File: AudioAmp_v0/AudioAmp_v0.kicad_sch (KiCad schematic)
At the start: 2 parts, among them J1 Conn_01x02_Pin, U1 MAU108

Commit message: 電源回路完成
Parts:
- added C1: 100u, symbol Device:C_Polarized
- added C2, C6, C7: 10u, Capacitor_SMD:C_0805_2012Metric, symbol Device:C
- added C3, C4, C5: 0.1u, Capacitor_SMD:C_0603_1608Metric, symbol Device:C
- J1: footprint (none) -> Connector_Molex:Molex_SPOX_5268-02A_1x02_P2.50mm_Horizontal
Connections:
- net +5V: now also U1.1 (+VIN), C1.1, C2.1, C3.1
- net GND: now also U1.2 (-Vin), U1.5 (Common), C1.2, C2.2, C3.2, C4.2, C5.1, C6.2, C7.1
- net +12V: now reaches U1.4 (-VOUT)
- net +12V: now also C4.1, C6.1
- net -12V: now reaches U1.6 (+Vout)
- net -12V: now also C5.2, C7.2
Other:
- moved on the sheet: U1

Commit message: アンプ回路ちょっと
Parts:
- added J2: AudioJack3, Connector_Audio:Jack_3.5mm_Switronic_ST-005-G_horizontal, symbol Connector_Audio:AudioJack3
- added RV1: R_Potentiometer_Dual, symbol Device:R_Potentiometer_Dual
- added U2: NJM5532, Package_DIP:DIP-8_W7.62mm, symbol Amplifier_Operational:NJM5532
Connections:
- net GND: now also J2.S
- new net: U2.1, U2.5 (+)
- new net: U2.6 (-), U2.7
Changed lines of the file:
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@@
+    (stroke (width 0) (type default))
+  )
+  (wire (pts (xy 90.17 119.38) (xy 90.17 124.46))
+    (stroke (width 0) (type default))
+  )
+  (wire (pts (xy 33.02 129.54) (xy 34.29 129.54))
     (stroke (width 0) (type default))
   )
@@
     (stroke (width 0) (type default))
   )
-  (wire (pts (xy 38.1 72.39) (xy 43.18 72.39))
+  (wire (pts (xy 87.63 128.27) (xy 87.63 114.3))
     (stroke (width 0) (type default))
   )
@@
     (stroke (width 0) (type default))
   )
+  (wire (pts (xy 90.17 124.46) (xy 107.95 124.46))
+    (stroke (width 0) (type default))
+  )
   (wire (pts (xy 118.11 81.28) (xy 128.27 81.28))
     (stroke (width 0) (type default))
@@
     (stroke (width 0) (type default))
   )
-  (wire (pts (xy 44.45 74.93) (xy 38.1 74.93))
+  (wire (pts (xy 87.63 114.3) (xy 90.17 114.3))
+    (stroke (width 0) (type default))
+  )
+  (wire (pts (xy 41.91 74.93) (xy 38.1 74.93))
+    (stroke (width 0) (type default))
+  )
+  (wire (pts (xy 107.95 124.46) (xy 107.95 116.84))
     (stroke (width 0) (type default))
   )
@@
     (stroke (width 0) (type default))
   )
+  (wire (pts (xy 86.36 128.27) (xy 87.63 128.27))
+    (stroke (width 0) (type default))
+  )
   (wire (pts (xy 118.11 63.5) (xy 128.27 63.5))
     (stroke (width 0) (type default))
@@
     (stroke (width 0) (type default))
   )
-  (wire (pts (xy 44.45 68.58) (xy 44.45 74.93))
-    (stroke (width 0) (type default))
-  )
   (wire (pts (xy 114.3 76.2) (xy 114.3 81.28))
     (stroke (width 0) (type default))
@@
     (stroke (width 0) (type default))
   )
+  (wire (pts (xy 38.1 72.39) (xy 41.91 72.39))
+    (stroke (width 0) (type default))
+  )
   (wire (pts (xy 72.39 68.58) (xy 81.28 68.58))
     (stroke (width 0) (type default))
   )
-  (wire (pts (xy 43.18 72.39) (xy 43.18 77.47))
+  (wire (pts (xy 107.95 116.84) (xy 105.41 116.84))
     (stroke (width 0) (type default))
   )
@@
     )
   )
+  (symbol (lib_id "Amplifier_Operational:NJM5532") (at 68.58 92.71 0) (unit 3)
+    (in_bom yes) (on_board yes) (dnp no) (fields_autoplaced)
+    (property "Reference" "U2" (at 67.31 91.44 0)
+      (effects (font (size 1.27 1.27)) (justify left))
+    )
+    (property "Value" "NJM5532" (at 67.31 93.98 0)
+      (effects (font (size 1.27 1.27)) (justify left))
+    )
+    (property "Footprint" "Package_DIP:DIP-8_W7.62mm" (at 68.58 92.71 0)
+      (effects (font (size 1.27 1.27)) hide)
+    )
+    (property "Datasheet" "http://www.njr.com/semicon/PDF/NJM5532_E.pdf" (at 68.58 92.71 0)
+      (effects (font (size 1.27 1.27)) hide)
+    )
+    (pin "1")
+    (pin "8")
+    (pin "4")
+    (pin "6")
+    (pin "7")
+    (pin "3")
+    (pin "5")
+    (pin "2")
+    (instances
+      (project "AudioAmp_v0"
+        (path "/4f57bce5-a0af-4dee-a148-d94d96167cd8"
+          (reference "U2") (unit 3)
+        )
+      )
+    )
+  )
   (symbol (lib_id "power:+5V") (at 58.42 67.31 0) (unit 1)
     (in_bom yes) (on_board yes) (dnp no) (fields_autoplaced)
@@
     )
   )
-  (symbol (lib_id "power:+5V") (at 44.45 68.58 0) (unit 1)
-    (in_bom yes) (on_board yes) (dnp no) (fields_autoplaced)
-    (property "Reference" "#PWR02" (at 44.45 72.39 0)
-      (effects (font (size 1.27 1.27)) hide)
-    )
-    (property "Value" "+5V" (at 44.45 63.5 0)
-      (effects (font (size 1.27 1.27)))
-    )
-    (property "Footprint" "" (at 44.45 68.58 0)
-      (effects (font (size 1.27 1.27)) hide)
-    )
-    (property "Datasheet" "" (at 44.45 68.58 0)
+  (symbol (lib_id "power:+5V") (at 41.91 74.93 270) (unit 1)
+    (in_bom yes) (on_board yes) (dnp no) (fields_autoplaced)
+    (property "Reference" "#PWR02" (at 38.1 74.93 0)
+      (effects (font (size 1.27 1.27)) hide)
+    )
+    (property "Value" "+5V" (at 45.72 74.93 90)
+      (effects (font (size 1.27 1.27)) (justify left))
+    )
+    (property "Footprint" "" (at 41.91 74.93 0)
+      (effects (font (size 1.27 1.27)) hide)
+    )
+    (property "Datasheet" "" (at 41.91 74.93 0)
       (effects (font (size 1.27 1.27)) hide)
     )
@@
     )
   )
+  (symbol (lib_id "Connector_Audio:AudioJack3") (at 27.94 132.08 0) (unit 1)
+    (in_bom yes) (on_board yes) (dnp no) (fields_autoplaced)
+    (property "Reference" "J2" (at 26.035 123.19 0)
+      (effects (font (size 1.27 1.27)))
+    )
+    (property "Value" "AudioJack3" (at 26.035 125.73 0)
+      (effects (font (size 1.27 1.27)))
+    )
+    (property "Footprint" "Connector_Audio:Jack_3.5mm_Switronic_ST-005-G_horizontal" (at 27.94 132.08 0)
+      (effects (font (size 1.27 1.27)) hide)
+    )
+    (property "Datasheet" "~" (at 27.94 132.08 0)
+      (effects (font (size 1.27 1.27)) hide)
+    )
+    (pin "R")
+    (pin "T")
+    (pin "S")
+    (instances
+      (project "AudioAmp_v0"
+        (path "/4f57bce5-a0af-4dee-a148-d94d96167cd8"
+          (reference "J2") (unit 1)
+        )
+      )
+    )
+  )
+  (symbol (lib_id "Device:R_Potentiometer_Dual") (at 59.69 114.3 270) (unit 1)
+    (in_bom yes) (on_board yes) (dnp no) (fields_autoplaced)
+    (property "Reference" "RV1" (at 54.61 113.03 90)
+      (effects (font (size 1.27 1.27)) (justify right))
+    )
+    (property "Value" "R_Potentiometer_Dual" (at 54.61 115.57 90)
+      (effects (font (size 1.27 1.27)) (justify right))
+    )
+    (property "Footprint" "" (at 57.785 120.65 0)
+      (effects (font (size 1.27 1.27)) hide)
+    )
+    (property "Datasheet" "~" (at 57.785 120.65 0)
+      (effects (font (size 1.27 1.27)) hide)
+    )
+    (pin "2")
+    (pin "5")
+    (pin "1")
+    (pin "6")
+    (pin "3")
+    (pin "4")
+    (instances
+      (project "AudioAmp_v0"
+        (path "/4f57bce5-a0af-4dee-a148-d94d96167cd8"
+          (reference "RV1") (unit 1)
+        )
+      )
+    )
+  )
   (symbol (lib_id "Device:C") (at 128.27 77.47 0) (unit 1)
     (in_bom yes) (on_board yes) (dnp no)
@@
     )
   )
+  (symbol (lib_id "power:GND") (at 34.29 129.54 90) (unit 1)
+    (in_bom yes) (on_board yes) (dnp no) (fields_autoplaced)
+    (property "Reference" "#PWR08" (at 40.64 129.54 0)
+      (effects (font (size 1.27 1.27)) hide)
+    )
+    (property "Value" "GND" (at 38.1 129.54 90)
+      (effects (font (size 1.27 1.27)) (justify right))
+    )
+    (property "Footprint" "" (at 34.29 129.54 0)
+      (effects (font (size 1.27 1.27)) hide)
+    )
+    (property "Datasheet" "" (at 34.29 129.54 0)
+      (effects (font (size 1.27 1.27)) hide)
+    )
+    (pin "1")
+    (instances
+      (project "AudioAmp_v0"
+        (path "/4f57bce5-a0af-4dee-a148-d94d96167cd8"
+          (reference "#PWR08") (unit 1)
+        )
+      )
+    )
+  )
+  (symbol (lib_id "Amplifier_Operational:NJM5532") (at 78.74 128.27 0) (unit 1)
+    (in_bom yes) (on_board yes) (dnp no) (fields_autoplaced)
+    (property "Reference" "U2" (at 78.74 118.11 0)
+      (effects (font (size 1.27 1.27)))
+    )
+    (property "Value" "NJM5532" (at 78.74 120.65 0)
+      (effects (font (size 1.27 1.27)))
+    )
+    (property "Footprint" "Package_DIP:DIP-8_W7.62mm" (at 78.74 128.27 0)
+      (effects (font (size 1.27 1.27)) hide)
+    )
+    (property "Datasheet" "http://www.njr.com/semicon/PDF/NJM5532_E.pdf" (at 78.74 128.27 0)
+      (effects (font (size 1.27 1.27)) hide)
+    )
+    (pin "1")
+    (pin "8")
+    (pin "4")
+    (pin "6")
+    (pin "7")
+    (pin "3")
+    (pin "5")
+    (pin "2")
+    (instances
+      (project "AudioAmp_v0"
+        (path "/4f57bce5-a0af-4dee-a148-d94d96167cd8"
+          (reference "U2") (unit 1)
+        )
+      )
+    )
+  )
+  (symbol (lib_id "Amplifier_Operational:NJM5532") (at 97.79 116.84 0) (unit 2)
+    (in_bom yes) (on_board yes) (dnp no) (fields_autoplaced)
+    (property "Reference" "U2" (at 97.79 106.68 0)
+      (effects (font (size 1.27 1.27)))
+    )
+    (property "Value" "NJM5532" (at 97.79 109.22 0)
+      (effects (font (size 1.27 1.27)))
+    )
+    (property "Footprint" "Package_DIP:DIP-8_W7.62mm" (at 97.79 116.84 0)
+      (effects (font (size 1.27 1.27)) hide)
+    )
+    (property "Datasheet" "http://www.njr.com/semicon/PDF/NJM5532_E.pdf" (at 97.79 116.84 0)
+      (effects (font (size 1.27 1.27)) hide)
+    )
+    (pin "1")
+    (pin "8")
+    (pin "4")
+    (pin "6")
+    (pin "7")
+    (pin "3")
+    (pin "5")
+    (pin "2")
+    (instances
+      (project "AudioAmp_v0"
+        (path "/4f57bce5-a0af-4dee-a148-d94d96167cd8"
+          (reference "U2") (unit 2)
+        )
+      )
+    )
+  )
   (symbol (lib_id "Device:C") (at 118.11 77.47 0) (unit 1)
     (in_bom yes) (on_board yes) (dnp no)
@@
     )
   )
-  (symbol (lib_id "power:GND") (at 43.18 77.47 0) (unit 1)
-    (in_bom yes) (on_board yes) (dnp no) (fields_autoplaced)
-    (property "Reference" "#PWR01" (at 43.18 83.82 0)
-      (effects (font (size 1.27 1.27)) hide)
-    )
-    (property "Value" "GND" (at 43.18 82.55 0)
-      (effects (font (size 1.27 1.27)))
-    )
-    (property "Footprint" "" (at 43.18 77.47 0)
-      (effects (font (size 1.27 1.27)) hide)
-    )
-    (property "Datasheet" "" (at 43.18 77.47 0)
-      (effects (font (size 1.27 1.27)) hide)
-    )
+  (symbol (lib_id "power:GND") (at 41.91 72.39 90) (unit 1)
+    (in_bom yes) (on_board yes) (dnp no) (fields_autoplaced)
+    (property "Reference" "#PWR01" (at 48.26 72.39 0)
+      (effects (font (size 1.27 1.27)) hide)
+    )
+    (property "Value" "GND" (at 45.72 72.39 90)
+      (effects (font (size 1.27 1.27)) (justify right))
+    )
+    (property "Footprint" "" (at 41.91 72.39 0)
+      (effects (font (size 1.27 1.27)) hide)
+    )
+    (property "Datasheet" "" (at 41.91 72.39 0)
+      (effects (font (size 1.27 1.27)) hide)
+    )

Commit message: アンプ回路一応完成
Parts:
- added C10, C11: 0.1u, Capacitor_THT:C_Rect_L13.0mm_W6.0mm_P10.00mm_FKS3_FKP3_MKS4, symbol Device:C
- added C4, C5: 2.2u, Capacitor_THT:C_Axial_L17.0mm_D7.0mm_P20.00mm_Horizontal, symbol Device:C
- added J3, J4: Connector_RCJ-042, TomoshibiLibrary:Connector_RCJ-042CUD, symbol TomoshibiLibrary:Connector_RCJ-042
- added J5: AudioJack3, Connector_Audio:Jack_3.5mm_Switronic_ST-005-G_horizontal, symbol Connector_Audio:AudioJack3
- added J6, J7: Conn_01x02_Pin, Connector_JST:JST_XH_S2B-XH-A_1x02_P2.50mm_Horizontal, symbol Connector:Conn_01x02_Pin
- added JP1, JP2: SolderJumper_3_Open, Jumper:SolderJumper-3_P2.0mm_Open_TrianglePad1.0x1.5mm, symbol Jumper:SolderJumper_3_Open
- added R1, R2: 1K, Resistor_THT:R_Axial_DIN0207_L6.3mm_D2.5mm_P10.16mm_Horizontal, symbol Device:R
- added R10, R9: 27K, Resistor_THT:R_Axial_DIN0207_L6.3mm_D2.5mm_P10.16mm_Horizontal, symbol Device:R
- added R11, R12, R13, R14: 47, Resistor_THT:R_Axial_DIN0207_L6.3mm_D2.5mm_P10.16mm_Horizontal, symbol Device:R
- added R15, R16: 22, Resistor_THT:R_Axial_DIN0207_L6.3mm_D2.5mm_P10.16mm_Horizontal, symbol Device:R
- added R3, R4: 22K, Resistor_THT:R_Axial_DIN0207_L6.3mm_D2.5mm_P10.16mm_Horizontal, symbol Device:R
- added R5, R6: 2.2K, Resistor_THT:R_Axial_DIN0207_L6.3mm_D2.5mm_P10.16mm_Horizontal, symbol Device:R
- added R7, R8: 10K, Resistor_THT:R_Axial_DIN0207_L6.3mm_D2.5mm_P10.16mm_Horizontal, symbol Device:R
- added SW1, SW3: SW_SPDT, TomoshibiLibrary:SW_Toggle_3P_SPDT_5Pin, symbol Switch:SW_SPDT
- added U3: NJM5532, Package_DIP:DIP-8_W7.62mm, symbol Amplifier_Operational:NJM5532
- C1: footprint (none) -> Capacitor_SMD:CP_Elec_6.3x5.7
- RV1: footprint (none) -> TomoshibiLibrary:VR_ALPS9-dual
- renumbered C4 to C6, C5 to C7, C6 to C8, C7 to C9, J2 to J1, J1 to J2
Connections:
- net +12V: now also JP1.1 (A)
- net -12V: now also JP2.1 (A)
- net GND: now also RV1.3, RV1.6, J3.1, J4.1, J5.S, J6.1 (Pin_1), J7.2 (Pin_2), R3.1, R4.1, R5.1, R6.1
- net VEE: now reaches U2.4 (V-)
- net VEE: now also JP2.2 (C), U3.4 (V-)
- net VCC: now reaches U2.8 (V+)
- net VCC: now also JP1.2 (C), U3.8 (V+)
- net at J1.R: now also RV1.4, J4.2
- net at J1.T: now also RV1.1, J3.2
- net at RV1.2: now also C4.1
- net at RV1.5: now also C5.1
- net at U2.1, U2.5 (+): now also R11.2
- net at U2.2 (-): now also R5.2, R7.2
- net at U2.3 (+): now also R1.2, R3.2
- net at U2.6 (-), U2.7: now also R13.2
- new net: C5.2, R2.1
- new net: C4.2, R1.1
- new net: J5.T, R15.1
- new net: C10.2, R11.1, R13.1, R15.2, R9.1, SW3.1 (A)
- new net: C11.2, R10.1, R12.1, R14.1, R16.2, SW1.1 (A)
- new net: C11.1, R10.2, R8.1, SW1.2 (B)
- new net: J5.R, R16.1
- new net: R12.2, U3.1, U3.5 (+)
- new net: R14.2, U3.6 (-), U3.7
- new net: R6.2, R8.2, U3.2 (-)
- new net: C10.1, R7.1, R9.2, SW3.2 (B)
- new net: R2.2, R4.2, U3.3 (+)
- new net +9V: J6.2 (Pin_2), JP1.3 (B)
- new net -9V: J7.1 (Pin_1), JP2.3 (B)
- no-connect marks 0 -> 2
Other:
- moved on the sheet: C1, C2, C3, C6, C7, C8, C9, J1, J2, RV1, U1, U2A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

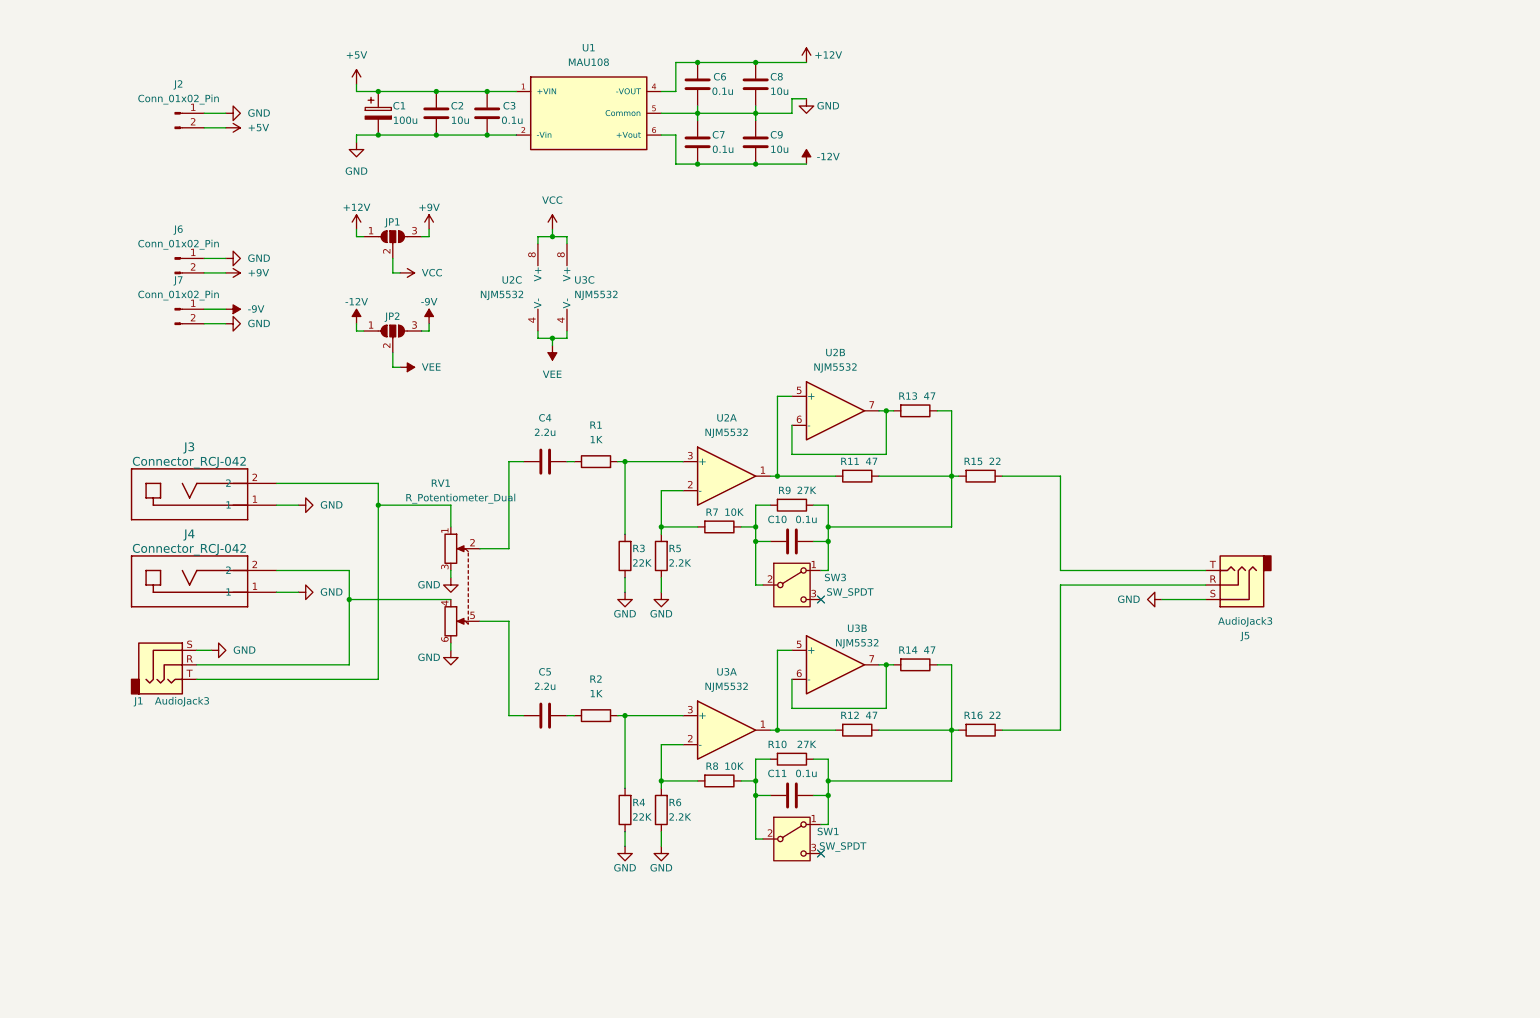
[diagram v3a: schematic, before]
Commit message: 電源切り替え回路を追加
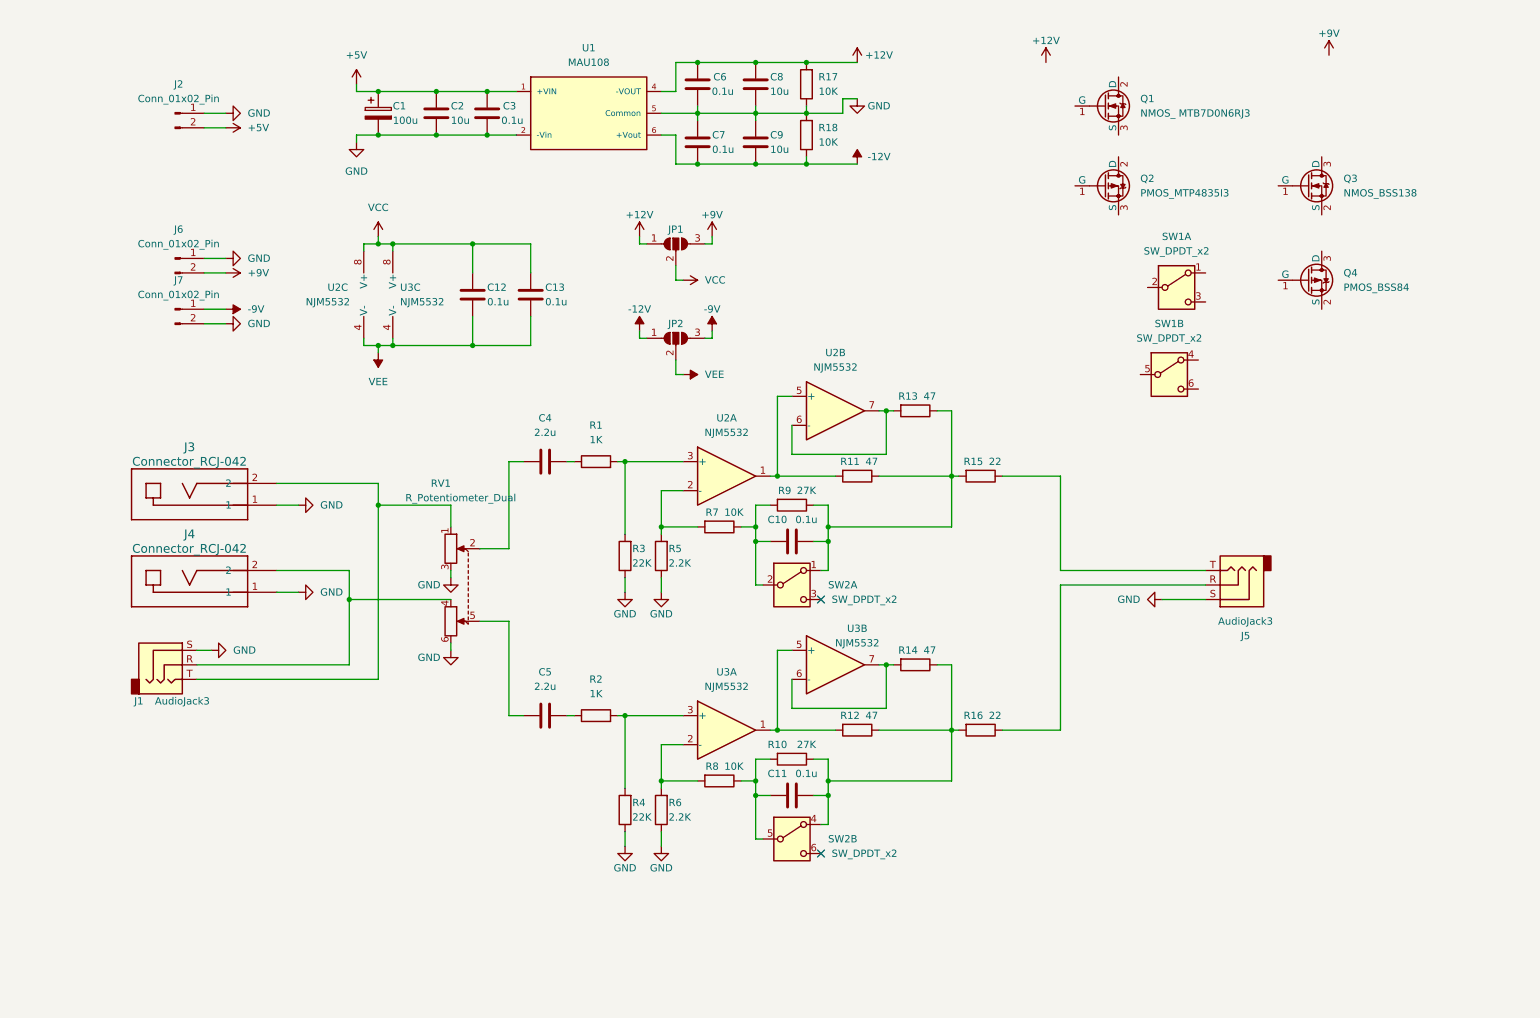
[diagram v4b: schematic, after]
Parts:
- removed SW1, SW3: SW_SPDT, TomoshibiLibrary:SW_Toggle_3P_SPDT_5Pin, symbol Switch:SW_SPDT
- added C12, C13: 0.1u, Capacitor_SMD:C_0603_1608Metric, symbol Device:C
- added Q1: NMOS_ MTB7D0N6RJ3, Package_TO_SOT_SMD:TO-252-2, symbol Device:Q_NMOS_GDS
- added Q2: PMOS_MTP4835I3, Package_TO_SOT_SMD:TO-252-2, symbol Device:Q_PMOS_GDS
- added Q3: NMOS_BSS138, Package_TO_SOT_SMD:SOT-23, symbol Device:Q_NMOS_GSD
- added Q4: PMOS_BSS84, Package_TO_SOT_SMD:TSOT-23, symbol Device:Q_PMOS_GSD
- added R17, R18: 10K, Resistor_THT:R_Axial_DIN0207_L6.3mm_D2.5mm_P10.16mm_Horizontal, symbol Device:R
- added SW1: SW_DPDT_x2, Button_Switch_THT:SW_CK_JS202011CQN_DPDT_Straight, symbol Switch:SW_DPDT_x2
- added SW2: SW_DPDT_x2, Button_Switch_THT:SW_E-Switch_EG2219_DPDT_Angled, symbol Switch:SW_DPDT_x2
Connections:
- net +12V: now also R17.2
- net -12V: now also R18.1
- net GND: now also R17.1, R18.2
- net VCC: now also C12.1, C13.1
- net VEE: now also C12.2, C13.2
- net at C10.2, R11.1, R13.1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: now also SW2.1 (A)
- net at C11.2, R10.1, R12.1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: now also SW2.4 (A)
- net at C11.1, R10.2, R8.1: now also SW2.5 (B)
- net at C10.1, R7.1, R9.2: now also SW2.2 (B)
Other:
- moved on the sheet: JP1, JP2, U2C, U3C
